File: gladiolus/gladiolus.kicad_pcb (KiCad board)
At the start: 4 copper layers, 70.7 x 53.3 mm, 137 parts, among them J1 NEIGHBOR1, J2 NEIGHBOR2, J7 BONUS_ROW, Q1 Q_NPN_BEC, U1 THS4520RGT, U2 AD8330ARQZ, U3 AD9283, U4 AD9704, U5 LMH6643, U6 74LVC1G3157, U7 74LVC1G3157

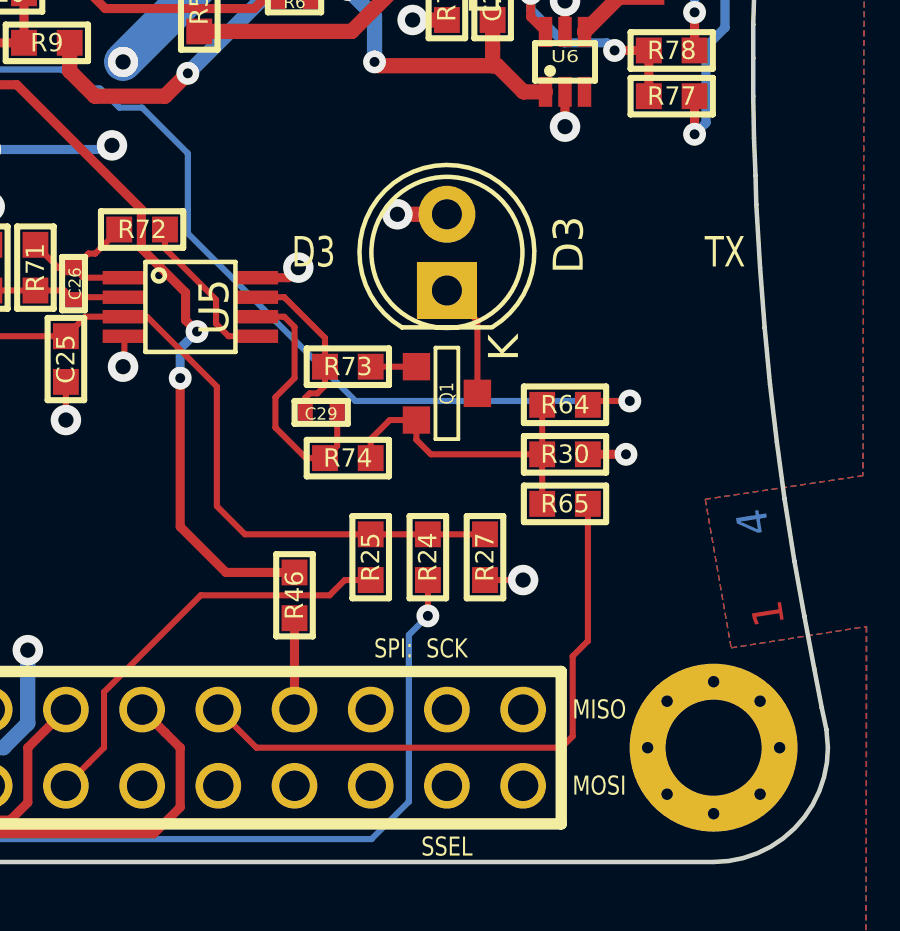
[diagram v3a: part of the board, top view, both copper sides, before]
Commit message: Minor change to Gladiolus silkscreen. Began designing Foxglove level shifters / comparators and power supplies.
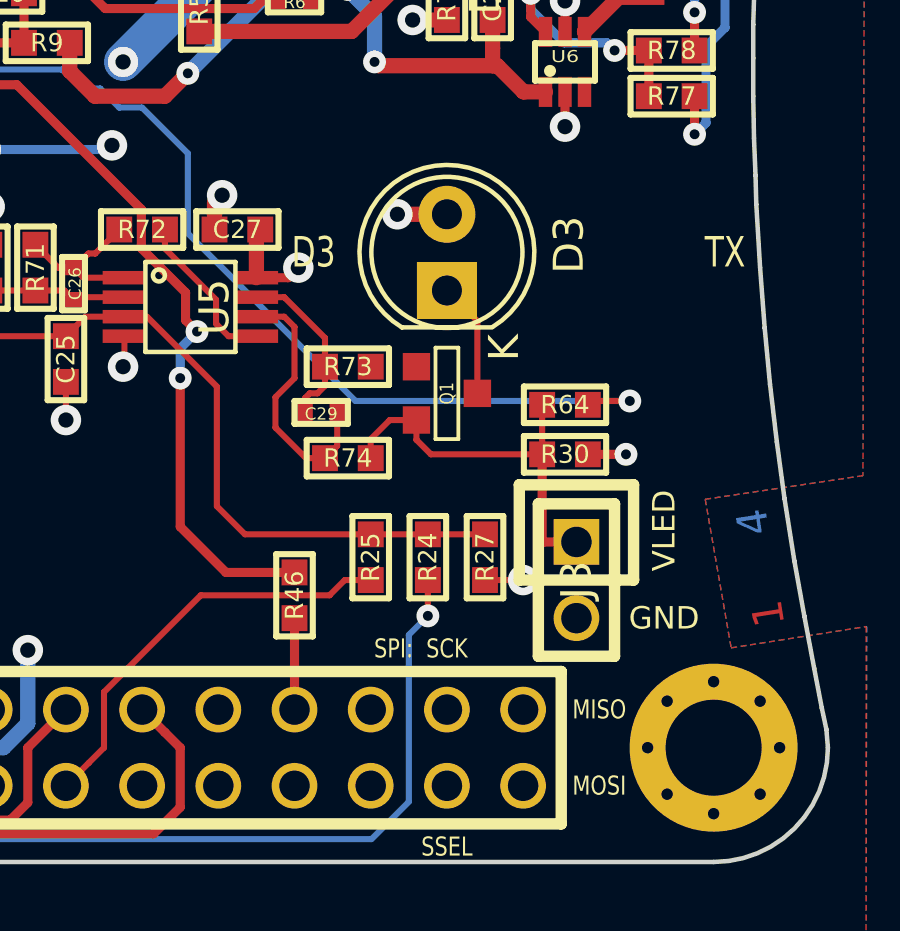
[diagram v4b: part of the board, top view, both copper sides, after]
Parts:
- removed R65: 0, gsg-modules:0603
- added C27: 100nF, gsg-modules:0603, F.Cu at (160.7, 100.8)
- added J3: Conn_01x02_Female, gsg-modules:HEADER-1x2, F.Cu at (172.0, 112.5)
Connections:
- J1 pad 10: /P1_1 -> (no net)
- J1 pad 11: /CLK0 -> (no net)
- J1 pad 12: /P1_2 -> (no net)
- J1 pad 24: /P5_4 -> (no net)
- J1 pad 29: /P5_7 -> (no net)
- J1 pad 3: /P4_9 -> (no net)
- J1 pad 31: /P1_18 -> (no net)
- J1 pad 32: /P1_17 -> (no net)
- J1 pad 33: /P9_5 -> (no net)
- J1 pad 35: /P2_0 -> (no net)
- J1 pad 36: /P6_0 -> (no net)
- J1 pad 37: /P1_20 -> (no net)
- J1 pad 38: /P1_19 -> (no net)
- J1 pad 39: /P1_4 -> (no net)
- J1 pad 40: /P1_3 -> (no net)
- J1 pad 5: /P4_10 -> (no net)
- J1 pad 9: /P5_1 -> (no net)
- J2 pad 10: /P4_6 -> (no net)
- J2 pad 11: /P4_7 -> (no net)
- J2 pad 12: /CLK2 -> (no net)
- J2 pad 13: /P2_8 -> (no net)
- J2 pad 14: /P2_7 -> (no net)
- J2 pad 15: /P2_6 -> (no net)
- J2 pad 16: /P7_7 -> (no net)
- J2 pad 17: /WAKEUP0 -> (no net)
- J2 pad 19: /P2_4 -> (no net)
- J2 pad 21: /PF_4 -> (no net)
- J2 pad 22: /P3_2 -> (no net)
- J2 pad 23: /P7_2 -> (no net)
- J2 pad 24: /P3_1 -> (no net)
- J2 pad 25: /P7_1 -> (no net)
- J2 pad 26: /P3_0 -> (no net)
- J2 pad 27: /P7_0 -> (no net)
- J2 pad 28: /P3_4 -> (no net)
- J2 pad 29: /P6_8 -> (no net)
- J2 pad 30: /P3_7 -> (no net)
- J2 pad 31: /P6_7 -> (no net)
- J2 pad 32: /P3_3 -> (no net)
- J2 pad 38: /P3_6 -> (no net)
- J2 pad 39: /I2C0_SDA -> (no net)
- J2 pad 4: /P4_0 -> (no net)
- J2 pad 40: /I2C0_SCL -> (no net)
- J2 pad 6: /P4_5 -> (no net)
- J2 pad 8: /P4_2 -> (no net)
- J7 pad 11: /RESET -> (no net)
- J7 pad 12: /VBAT -> (no net)
- J7 pad 13: /P2_11 -> (no net)
- J7 pad 14: /P2_10 -> (no net)
- J7 pad 15: /P6_10 -> (no net)
- J7 pad 16: /P6_9 -> (no net)
- J7 pad 17: /P6_2 -> (no net)
- J7 pad 18: /P6_1 -> (no net)
- J7 pad 2: /P6_4 -> (no net)
- J7 pad 20: Net-(J7-Pad20) -> (no net)
- J7 pad 3: /P6_5 -> (no net)
- J7 pad 4: /ADC0_5 -> (no net)
- J7 pad 5: /ADC0_2 -> (no net)
- J7 pad 6: /P2_9 -> (no net)
- J7 pad 7: /P2_12 -> (no net)
- J7 pad 8: /P2_13 -> (no net)
- J7 pad 9: /RTC_ALARM -> (no net)
- U1 pad 1: Net-(U1-Pad1) -> (no net)
- U4 pad 13: Net-(U4-Pad13) -> (no net)
- U4 pad 4: Net-(U4-Pad4) -> (no net)
- U4 pad 5: Net-(U4-Pad5) -> (no net)
- U4 pad 6: Net-(U4-Pad6) -> (no net)
- U4 pad 7: Net-(U4-Pad7) -> (no net)
- U4 pad 8: Net-(U4-Pad8) -> (no net)
- U4 pad 9: Net-(U4-Pad9) -> (no net)
- U6 pad 3: Net-(U6-Pad3) -> (no net)
- U7 pad 3: Net-(U7-Pad3) -> (no net)
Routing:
- net /P1_17: track 20.5 -> 0.00 mm
- net Net-(J3-Pad1): track 10.8 -> 13.1 mm
- net VCC: track 137.7 -> 139.4 mm
- net Net-(Q1-Pad1): track 1.52 -> 0.00 mm
- net GND: track 88.0 -> 89.2 mm, vias 42 -> 43
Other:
- board text added: "VLED"

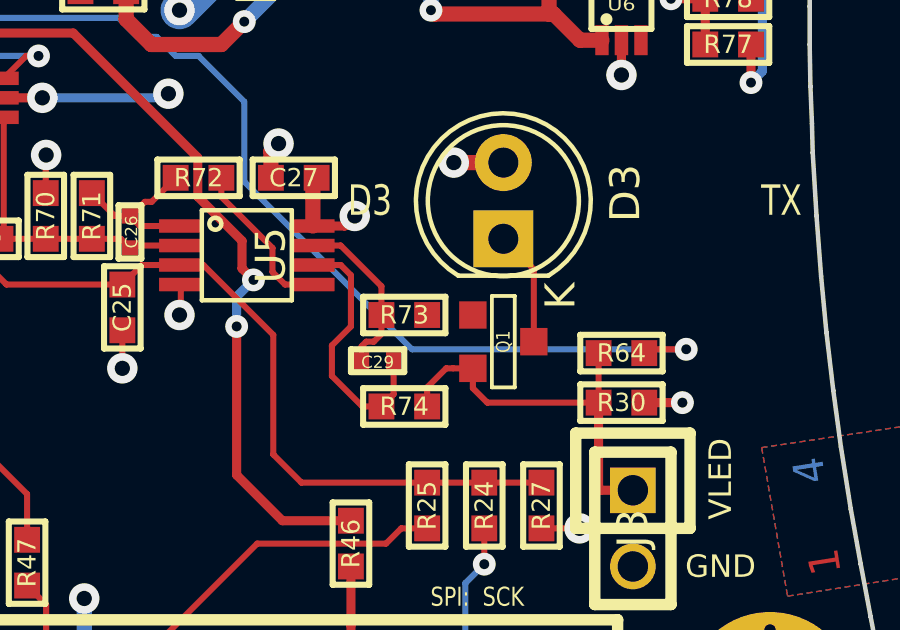
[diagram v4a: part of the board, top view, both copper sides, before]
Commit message: Lucky Bamboo: Rerouted RX RF signals and rearranged schematic to be consistent with layout. Gladiolus: Routed incomplete signal near TX transistor.
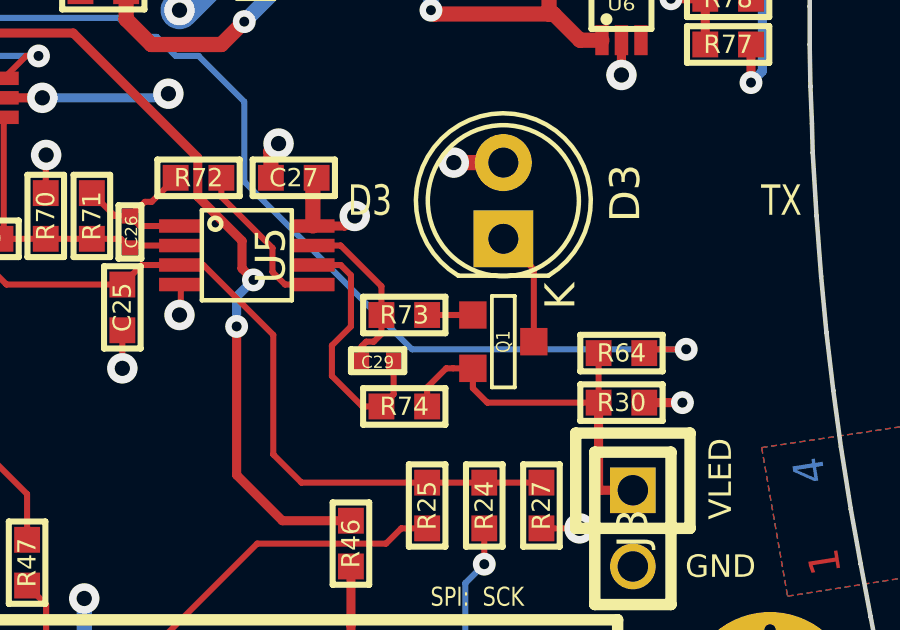
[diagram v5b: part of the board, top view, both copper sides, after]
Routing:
- net Net-(Q1-Pad1): track 0.00 -> 1.52 mm
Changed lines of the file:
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@@
     (thickness 1.6)
     (drawings 133)
-    (tracks 1067)
+    (tracks 1068)
     (zones 0)
     (modules 138)
@@
   )
   (setup
-    (last_trace_width 0.3048)
+    (last_trace_width 0.2032)
     (user_trace_width 0.3048)
     (user_trace_width 0.508)
@@
   (segment (start 172.212 83.90342) (end 170.39042 85.725) (width 0.3048) (layer F.Cu) (net 1))
   (segment (start 172.212 83.185) (end 172.212 83.90342) (width 0.3048) (layer F.Cu) (net 1))
+  (via (at 160.147 99.695) (size 1.016) (drill 0.508) (layers F.Cu B.Cu) (net 1))
+  (segment (start 159.893 100.838) (end 159.893 99.949) (width 0.508) (layer F.Cu) (net 1))
+  (segment (start 159.893 99.949) (end 160.147 99.695) (width 0.508) (layer F.Cu) (net 1))
   (segment (start 142.494 82.55) (end 146.558 78.486) (width 1.27) (layer B.Cu) (net 2))
   (segment (start 146.558 78.486) (end 147.828 78.486) (width 1.27) (layer B.Cu) (net 2))
@@
   (segment (start 170.434 84.49858) (end 171.069 85.13358) (width 0.3048) (layer B.Cu) (net 2))
   (segment (start 171.069 85.13358) (end 171.069 85.919054) (width 0.3048) (layer B.Cu) (net 2))
+  (segment (start 161.29 100.965) (end 161.417 100.838) (width 0.508) (layer F.Cu) (net 2))
+  (segment (start 161.29 102.444) (end 161.29 100.965) (width 0.508) (layer F.Cu) (net 2))
   (segment (start 121.92 71.12) (end 123.088401 69.951599) (width 0.508) (layer F.Cu) (net 3) (status 10))
   (segment (start 123.088401 69.951599) (end 170.740833 69.951599) (width 0.508) (layer F.Cu) (net 3))
@@
   (segment (start 139.315 88.575) (end 137.8764 88.575) (width 0.3048) (layer F.Cu) (net 56) (status 30))
   (segment (start 137.8764 88.575) (end 137.6934 88.392) (width 0.3048) (layer F.Cu) (net 56) (status 30))
-  (segment (start 170.815 108.331) (end 167.1066 108.331) (width 0.2032) (layer F.Cu) (net 101) (status 10))
-  (segment (start 167.1066 108.331) (end 166.624 107.8484) (width 0.2032) (layer F.Cu) (net 101))
-  (segment (start 166.624 107.8484) (end 166.624 107.188) (width 0.2032) (layer F.Cu) (net 101) (status 20))
-  (segment (start 165.9636 107.188) (end 166.624 107.188) (width 0.2032) (layer F.Cu) (net 101) (status 20))
-  (segment (start 165.735 107.188) (end 165.9636 107.188) (width 0.2032) (layer F.Cu) (net 101))
-  (segment (start 165.1 107.823) (end 165.735 107.188) (width 0.2032) (layer F.Cu) (net 101))
-  (segment (start 165.1 108.458) (end 165.1 107.823) (width 0.2032) (layer F.Cu) (net 101) (status 10))
-  (segment (start 170.815 108.331) (end 170.815 106.68) (width 0.2032) (layer F.Cu) (net 101) (status 30))
+  (segment (start 165.1 105.41) (end 166.624 105.41) (width 0.2032) (layer F.Cu) (net 57))
   (segment (start 163.31 90.5) (end 163.31 90.8946) (width 0.3048) (layer F.Cu) (net 58) (status 30))
   (segment (start 155.067 95.5548) (end 155.9052 96.393) (width 0.508) (layer F.Cu) (net 58))
@@
   (segment (start 163.322 106.299) (end 163.576 106.045) (width 0.2032) (layer F.Cu) (net 99))
   (segment (start 163.068 106.299) (end 163.322 106.299) (width 0.2032) (layer F.Cu) (net 99))
-  (via (at 160.147 99.695) (size 1.016) (drill 0.508) (layers F.Cu B.Cu) (net 1))
-  (segment (start 159.893 100.838) (end 159.893 99.949) (width 0.508) (layer F.Cu) (net 1))
-  (segment (start 159.893 99.949) (end 160.147 99.695) (width 0.508) (layer F.Cu) (net 1))
-  (segment (start 161.29 100.965) (end 161.417 100.838) (width 0.508) (layer F.Cu) (net 2))
-  (segment (start 161.29 102.444) (end 161.29 100.965) (width 0.508) (layer F.Cu) (net 2))
   (segment (start 143.8802 103.6) (end 144.1662 103.886) (width 0.2032) (layer F.Cu) (net 100))
   (segment (start 143.002 103.6) (end 143.8802 103.6) (width 0.2032) (layer F.Cu) (net 100) (status 10))
@@
   (segment (start 147.193 103.886) (end 148.209 102.87) (width 0.2032) (layer F.Cu) (net 100))
   (segment (start 148.209 102.87) (end 149.352 102.87) (width 0.2032) (layer F.Cu) (net 100) (status 20))
+  (segment (start 170.815 108.331) (end 167.1066 108.331) (width 0.2032) (layer F.Cu) (net 101) (status 10))
+  (segment (start 167.1066 108.331) (end 166.624 107.8484) (width 0.2032) (layer F.Cu) (net 101))
+  (segment (start 166.624 107.8484) (end 166.624 107.188) (width 0.2032) (layer F.Cu) (net 101) (status 20))
+  (segment (start 165.9636 107.188) (end 166.624 107.188) (width 0.2032) (layer F.Cu) (net 101) (status 20))
+  (segment (start 165.735 107.188) (end 165.9636 107.188) (width 0.2032) (layer F.Cu) (net 101))
+  (segment (start 165.1 107.823) (end 165.735 107.188) (width 0.2032) (layer F.Cu) (net 101))
+  (segment (start 165.1 108.458) (end 165.1 107.823) (width 0.2032) (layer F.Cu) (net 101) (status 10))
+  (segment (start 170.815 108.331) (end 170.815 106.68) (width 0.2032) (layer F.Cu) (net 101) (status 30))
   (segment (start 170.8912 111.252) (end 171.958 111.252) (width 0.3048) (layer F.Cu) (net 101))
   (segment (start 170.815 111.1758) (end 170.8912 111.252) (width 0.3048) (layer F.Cu) (net 101))

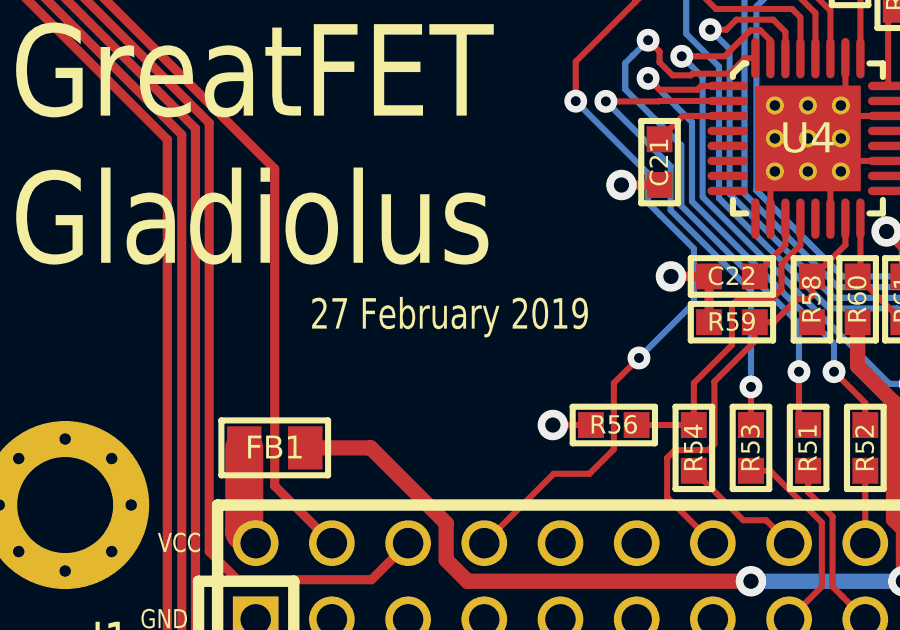
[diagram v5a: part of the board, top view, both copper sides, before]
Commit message: Replaced rescued symbols on Gladiolus and Lucky Bamboo. Lucky Bamboo: Shorted IRQ1/IRQ2 jumpers to create default connections.
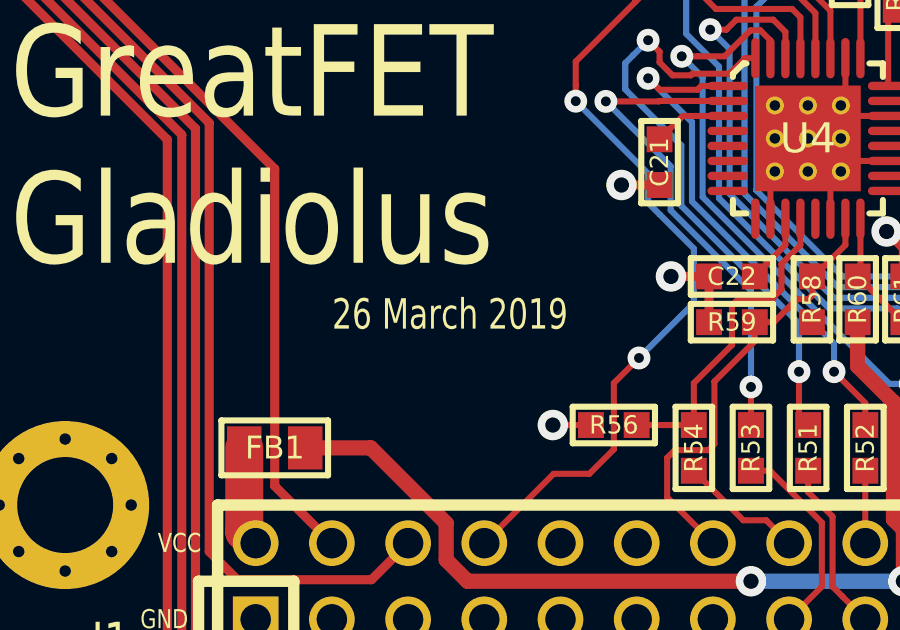
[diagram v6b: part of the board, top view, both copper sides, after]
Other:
- board text added: "26 March 2019"
- board text removed: "27 February 2019"
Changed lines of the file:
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@@
   (gr_line (start 177.9016 92.3544) (end 177.8508 94.0054) (angle 90) (layer Edge.Cuts) (width 0.15))
   (gr_line (start 177.9524 90.5002) (end 177.9016 92.3544) (angle 90) (layer Edge.Cuts) (width 0.15))
-  (gr_text "27 February 2019" (at 128.397 109.22) (layer F.SilkS)
+  (gr_text "26 March 2019" (at 128.397 109.22) (layer F.SilkS)
     (effects (font (size 1.016 0.762) (thickness 0.1524)))
   )
